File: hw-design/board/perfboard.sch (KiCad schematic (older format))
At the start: 8 parts, among them P10 CONN_01X16, P11 CONN_01X16, P12 CONN_01X16, P5 CONN_01X16, P6 CONN_01X16, P7 CONN_01X16, P8 CONN_01X16, P9 CONN_01X16

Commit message: adding footprint to local project directory (submodule)
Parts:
- P10, P11, P12, P5, P6, P7, P8, P9: footprint (none) -> Pin_Headers:Pin_Header_Angled_1x16
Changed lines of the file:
@@
 F 0 "P5" H 2350 3200 50  0000 C CNN
 F 1 "CONN_01X16" V 2450 2350 50  0000 C CNN
-F 2 "" H 2350 2350 60  0000 C CNN
+F 2 "Pin_Headers:Pin_Header_Angled_1x16" V 2350 2350 60  0000 C CNN
 F 3 "" H 2350 2350 60  0000 C CNN
 	1    2350 2350
@@
 F 0 "P6" H 2800 3200 50  0000 C CNN
 F 1 "CONN_01X16" V 2900 2350 50  0000 C CNN
-F 2 "" H 2800 2350 60  0000 C CNN
+F 2 "Pin_Headers:Pin_Header_Angled_1x16" V 2800 2350 60  0000 C CNN
 F 3 "" H 2800 2350 60  0000 C CNN
 	1    2800 2350
@@
 F 0 "P7" H 3250 3200 50  0000 C CNN
 F 1 "CONN_01X16" V 3350 2350 50  0000 C CNN
-F 2 "" H 3250 2350 60  0000 C CNN
+F 2 "Pin_Headers:Pin_Header_Angled_1x16" V 3250 2350 60  0000 C CNN
 F 3 "" H 3250 2350 60  0000 C CNN
 	1    3250 2350
@@
 F 0 "P8" H 3700 3200 50  0000 C CNN
 F 1 "CONN_01X16" V 3800 2350 50  0000 C CNN
-F 2 "" H 3700 2350 60  0000 C CNN
+F 2 "Pin_Headers:Pin_Header_Angled_1x16" V 3700 2350 60  0000 C CNN
 F 3 "" H 3700 2350 60  0000 C CNN
 	1    3700 2350
@@
 F 0 "P9" H 4150 3200 50  0000 C CNN
 F 1 "CONN_01X16" V 4250 2350 50  0000 C CNN
-F 2 "" H 4150 2350 60  0000 C CNN
+F 2 "Pin_Headers:Pin_Header_Angled_1x16" V 4150 2350 60  0000 C CNN
 F 3 "" H 4150 2350 60  0000 C CNN
 	1    4150 2350
@@
 F 0 "P10" H 4600 3200 50  0000 C CNN
 F 1 "CONN_01X16" V 4700 2350 50  0000 C CNN
-F 2 "" H 4600 2350 60  0000 C CNN
+F 2 "Pin_Headers:Pin_Header_Angled_1x16" V 4600 2350 60  0000 C CNN
 F 3 "" H 4600 2350 60  0000 C CNN
 	1    4600 2350
@@
 F 0 "P11" H 5050 3200 50  0000 C CNN
 F 1 "CONN_01X16" V 5150 2350 50  0000 C CNN
-F 2 "" H 5050 2350 60  0000 C CNN
+F 2 "Pin_Headers:Pin_Header_Angled_1x16" V 5050 2350 60  0000 C CNN
 F 3 "" H 5050 2350 60  0000 C CNN
 	1    5050 2350
@@
 F 0 "P12" H 5500 3200 50  0000 C CNN
 F 1 "CONN_01X16" V 5600 2350 50  0000 C CNN
-F 2 "" H 5500 2350 60  0000 C CNN
+F 2 "Pin_Headers:Pin_Header_Angled_1x16" V 5500 2350 60  0000 C CNN
 F 3 "" H 5500 2350 60  0000 C CNN
 	1    5500 2350

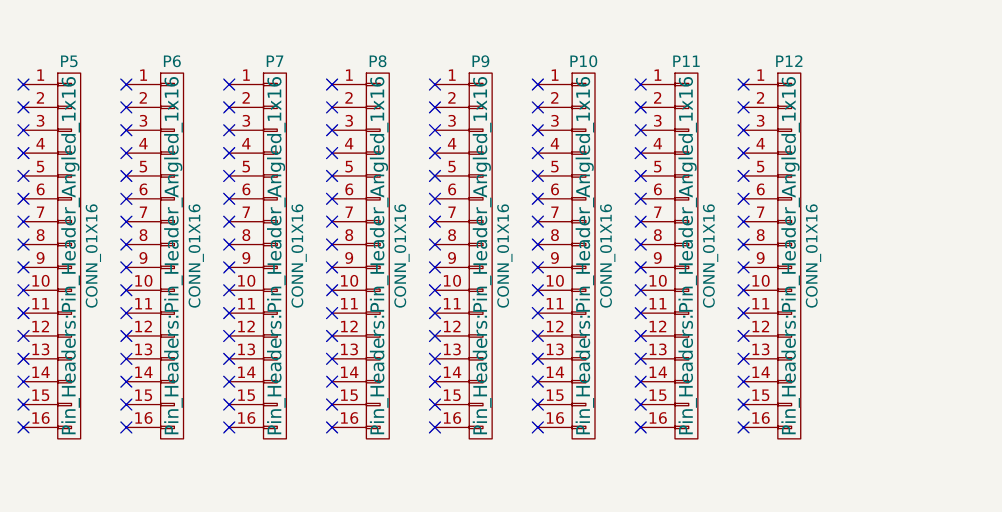
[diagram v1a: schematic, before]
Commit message: sch: fixing footprints and renaming some connectors
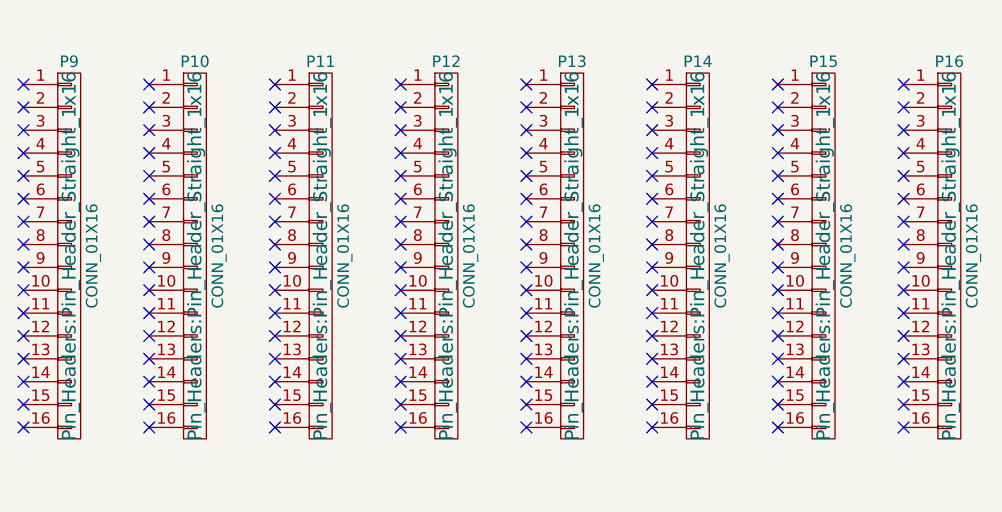
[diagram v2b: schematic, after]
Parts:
- removed P6, P7, P8, P9: CONN_01X16, Pin_Headers:Pin_Header_Angled_1x16, symbol CONN_01X16
- added P13, P14, P15, P16: CONN_01X16, Pin_Headers:Pin_Header_Straight_1x16, symbol CONN_01X16
- P10, P11, P12: footprint Pin_Headers:Pin_Header_Angled_1x16 -> Pin_Headers:Pin_Header_Straight_1x16
- P9: renamed from P5; footprint Pin_Headers:Pin_Header_Angled_1x16 -> Pin_Headers:Pin_Header_Straight_1x16

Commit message: sch: adjusting perfboard
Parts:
- removed P10, P11, P12, P13, P14, P15, P16: CONN_01X16, Pin_Headers:Pin_Header_Straight_1x16, symbol CONN_01X16
- added P10: Power, Socket_Arduino_Uno:Socket_Strip_Arduino_1x08, symbol CONN_01X08
- added P11: Analog, Socket_Arduino_Uno:Socket_Strip_Arduino_1x06, symbol CONN_01X06
- added P12: Digital, Socket_Arduino_Uno:Socket_Strip_Arduino_1x10, symbol CONN_01X10
- added P13: Digital, Socket_Arduino_Uno:Socket_Strip_Arduino_1x08, symbol CONN_01X08
- added P14, P15, P16, P17, P18, P19, P20, P21: ~, Pin_Headers:Pin_Header_Straight_1x14, symbol CONN_01X14
- P9: value CONN_01X16 -> ~; footprint Pin_Headers:Pin_Header_Straight_1x16 -> Pin_Headers:Pin_Header_Straight_1x14; symbol CONN_01X16 -> CONN_01X14
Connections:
- new net +3V3: P10.4 (P4), P19.1 (P1), P19.10 (P10), P19.11 (P11), P19.12 (P12), P19.13 (P13), P19.14 (P14), P19.2 (P2), P19.3 (P3), P19.4 (P4), P19.5 (P5), P19.6 (P6), P19.7 (P7), P19.8 (P8), P19.9 (P9)
- new net +5V: P10.5 (P5), P20.1 (P1), P20.10 (P10), P20.11 (P11), P20.12 (P12), P20.13 (P13), P20.14 (P14), P20.2 (P2), P20.3 (P3), P20.4 (P4), P20.5 (P5), P20.6 (P6), P20.7 (P7), P20.8 (P8), P20.9 (P9)
- new net +9V: P10.8 (P8)
- new net AD0: P11.6 (P6)
- new net AD1: P11.5 (P5)
- new net AD2: P11.4 (P4)
- new net AD3: P11.3 (P3)
- new net AD4/SDA: P11.2 (P2), P12.9 (P9)
- new net AD5/SCL: P11.1 (P1), P12.10 (P10)
- new net AREF: P12.8 (P8)
- new net GNDD: P10.6 (P6), P10.7 (P7), P12.7 (P7), P21.1 (P1), P21.10 (P10), P21.11 (P11), P21.12 (P12), P21.13 (P13), P21.14 (P14), P21.2 (P2), P21.3 (P3), P21.4 (P4), P21.5 (P5), P21.6 (P6), P21.7 (P7), P21.8 (P8), P21.9 (P9)
- new net IO0/RXD: P13.1 (P1)
- new net IO1/TXD: P13.2 (P2)
- new net IO10/SS: P12.3 (P3)
- new net IO11/MOSI: P12.4 (P4)
- new net IO12/MISO: P12.5 (P5)
- new net IO13/SCK: P12.6 (P6)
- new net IO2: P13.3 (P3)
- new net IO3: P13.4 (P4)
- new net IO4: P13.5 (P5)
- new net IO5: P13.6 (P6)
- new net IO6: P13.7 (P7)
- new net IO7: P13.8 (P8)
- new net IO8: P12.1 (P1)
- new net IO9: P12.2 (P2)
- new net IOREF: P10.2 (P2)
- new net RESET: P10.3 (P3)
- no-connect marks 128 -> 102
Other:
- note added: "EXTRA HOLE FOR SIGNALS"
- note added: "PROTOTYPING AREA"
